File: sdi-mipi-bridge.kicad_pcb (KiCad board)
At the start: 6 copper layers, 70 x 42 mm, 204 parts, among them J1 112740-13, J2 112740-13, J3 WE_68715014522_ONE-SIDE, J4 GRPB052VWVN-RC, J5 GRPB041VWVN-RC, J6 GRPB052VWVN-RC, SW1 SW_DIP_x06, SW2 SW_DIP_x06, U1 MAX8902B, U2 GS2971A, U3 GS2988, U4 CrossLink_LIF-MD6000-6JMG80I, U5 SC18IS602BIPW, Y1 ABM7_27.000MH_D2Y_T

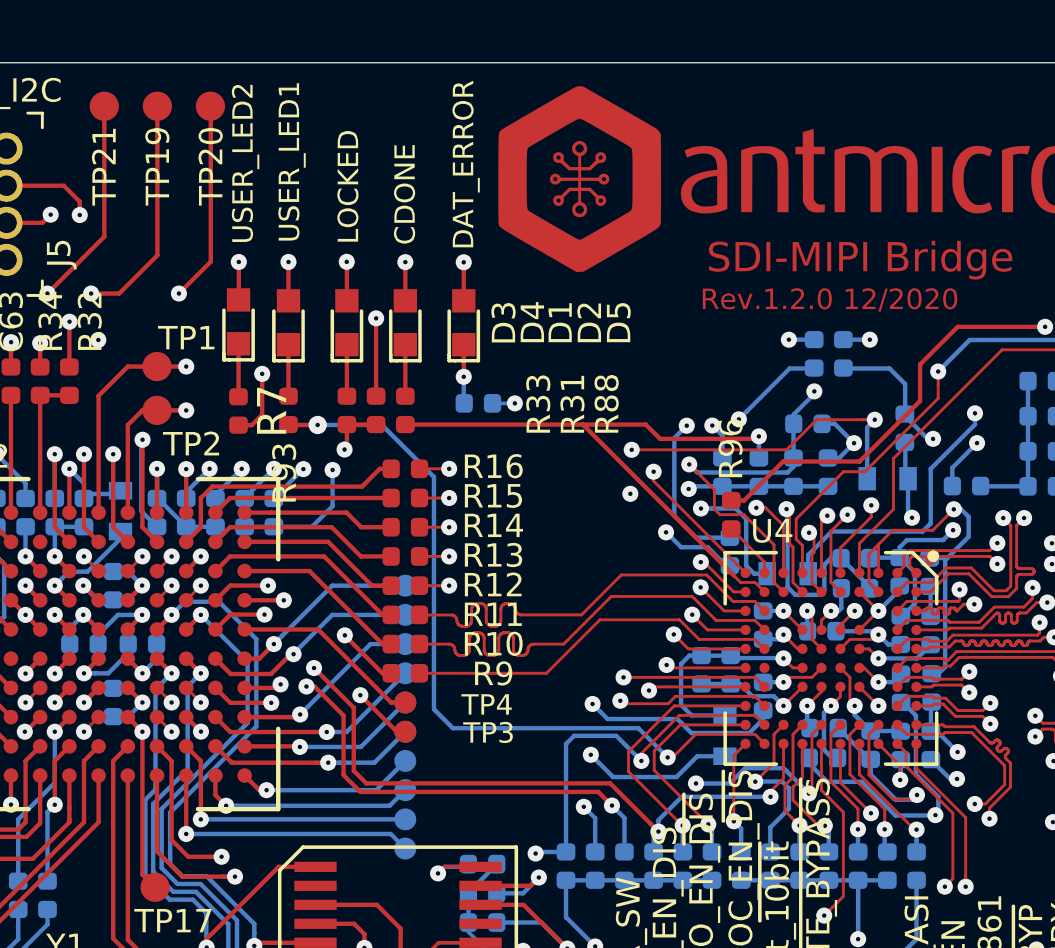
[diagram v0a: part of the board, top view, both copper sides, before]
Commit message: Change data pins routing
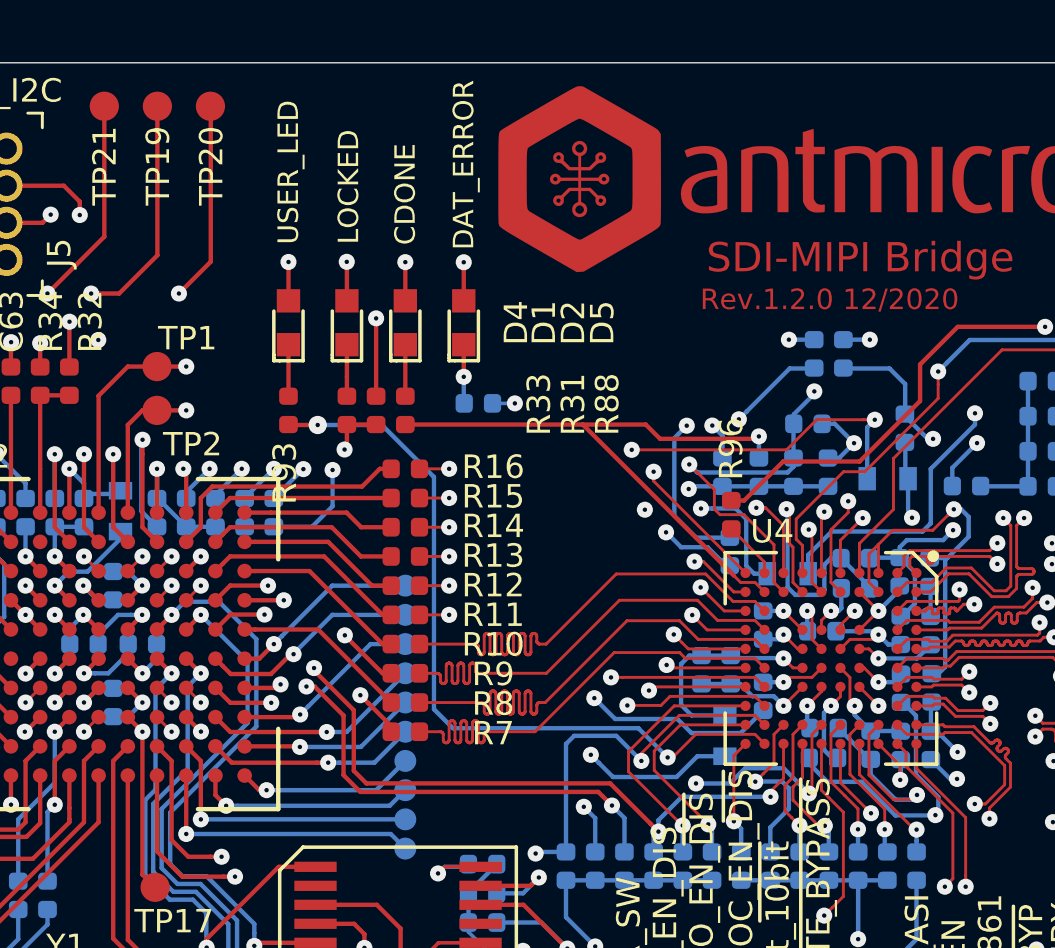
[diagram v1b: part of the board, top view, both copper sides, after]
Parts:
- removed D3: LG_L29K-G2J1-24-Z, sdi-mipi-bridge-footprints:LED_0603
- removed TP3, TP4: TP_SMD_0_75MM, sdi-mipi-bridge-footprints:Testpoint_smd_0_75mm
- added R8: R_0R_0402, sdi-mipi-bridge-footprints:0402-res, F.Cu at (131.0, 117.4)
- R7: value R_100R_0402 -> R_0R_0402
- moved R7 12.4 mm to (131.0, 118.4), turned to 180 degrees
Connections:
- net /USER_LED1 renamed /USER_LED
- R10 pad 1: /DOUT13 -> /DOUT14
- R10 pad 2: /D13 -> /D14
- R11 pad 1: /DOUT14 -> /DOUT10
- R11 pad 2: /D14 -> /D10
- R7 pad 1: Net-(D3-Pad1) -> /DOUT11
- R7 pad 2: /USER_LED2 -> /D11
- R9 pad 1: /DOUT12 -> /DOUT13
- R9 pad 2: /D12 -> /D13
- U2 pad C10: /D13 -> /D14
- U2 pad C8: /D12 -> /D13
- U2 pad C9: /D14 -> /D10
- U2 pad E10: Net-(TP4-Pad1) -> /D12
- U2 pad E9: Net-(TP3-Pad1) -> /D11
- U4 pad E1: /USER_LED2 -> /DOUT10
- U4 pad J6: Net-(U4-PadJ6) -> /DOUT11
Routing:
- net /USER_LED2: track 31.3 -> 0.00 mm, vias 2 -> 0
- net /DOUT10: track 0.00 -> 18.7 mm, vias 0 -> 2
- net /DOUT11: track 0.00 -> 17.8 mm
- net Net-(TP3-Pad1): track 8.37 -> 0.00 mm, vias 2 -> 0
- net /D11: track 0.00 -> 8.00 mm, vias 0 -> 2
- net /D10: track 0.00 -> 7.05 mm
- net /DOUT12: track 13.0 -> 19.7 mm
- net Net-(TP4-Pad1): track 6.53 -> 0.00 mm
- net /DOUT14: track 15.2 -> 19.7 mm
- net /DOUT19: track 13.2 -> 17.2 mm
- net /DOUT15: track 16.3 -> 20.2 mm
- net /DOUT16: track 15.3 -> 19.2 mm
- net /DOUT17: track 16.8 -> 20.6 mm
- net /DOUT18: track 15.8 -> 19.6 mm
- net /D13: track 6.05 -> 8.88 mm, vias 0 -> 2
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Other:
- board text added: "USER_LED"
- board text removed: "USER_LED1"
- board text removed: "USER_LED2"

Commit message: Update PCB, DRC clean
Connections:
- R10 pad 1: /DOUT14 -> /DOUT13
- R10 pad 2: /D14 -> /D13
- R11 pad 1: /DOUT10 -> /DOUT14
- R11 pad 2: /D10 -> /D14
- R7 pad 1: /DOUT11 -> /DOUT10
- R7 pad 2: /D11 -> /D10
- R8 pad 1: /DOUT12 -> /DOUT11
- R8 pad 2: /D12 -> /D11
- R9 pad 1: /DOUT13 -> /DOUT12
- R9 pad 2: /D13 -> /D12
- U2 pad C10: /D14 -> /D13
- U2 pad C8: /D13 -> /D12
- U2 pad C9: /D10 -> /D14
- U2 pad E10: /D12 -> /D11
- U2 pad E9: /D11 -> /D10
- U4 pad E1: /DOUT10 -> /DOUT14
- U4 pad J3: /DOUT14 -> /DOUT13
- U4 pad J4: /DOUT13 -> /DOUT12
- U4 pad J5: /DOUT12 -> /DOUT11
- U4 pad J6: /DOUT11 -> /DOUT10
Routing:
- net /D13: track 8.88 -> 6.05 mm, vias 2 -> 0
- net /D12: track 6.05 -> 8.88 mm, vias 0 -> 2
- net /DOUT13: track 16.9 -> 19.7 mm
- net /DOUT12: track 19.7 -> 16.9 mm
- net /D11: track 8.00 -> 6.05 mm, vias 2 -> 0
- net /DOUT11: track 17.8 -> 19.7 mm
- net /D14: track 6.05 -> 7.05 mm
- net /DOUT14: track 19.7 -> 18.7 mm, vias 0 -> 2
- net /DOUT10: track 18.7 -> 17.8 mm, vias 2 -> 0
- net /D10: track 7.05 -> 8.00 mm, vias 0 -> 2

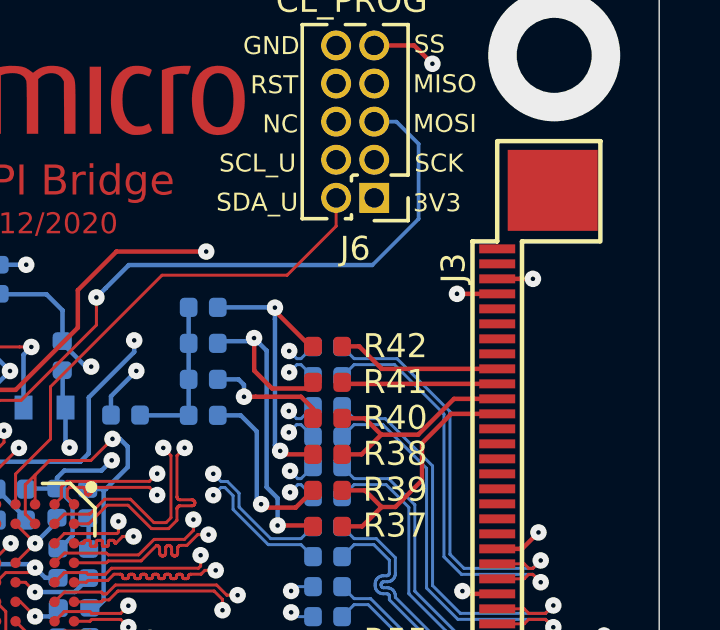
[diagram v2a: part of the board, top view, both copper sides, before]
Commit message: Add 0R resistor on 3.3v input to allow FFC to be disconnected from net
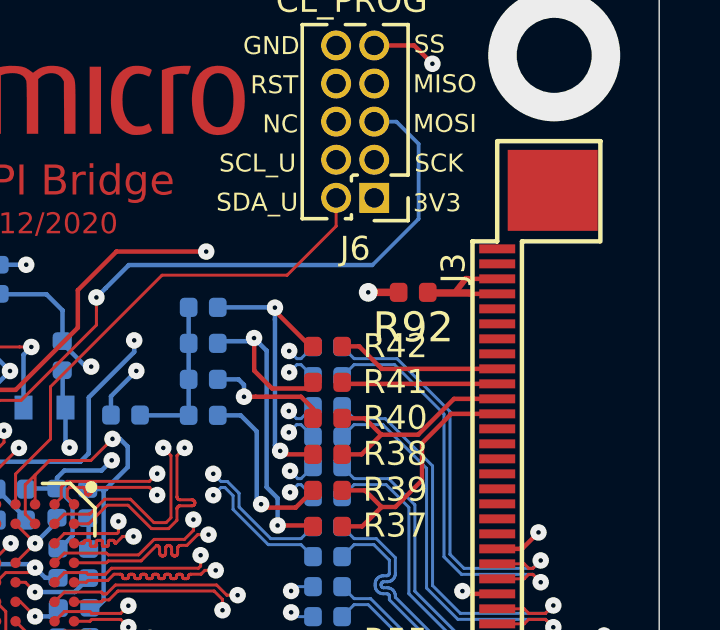
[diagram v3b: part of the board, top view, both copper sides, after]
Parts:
- added R92: R_0R_0402, sdi-mipi-bridge-footprints:0402-res, F.Cu at (159.8, 105.9)
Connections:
- J3 pad 47: +3V3 -> Net-(J3-Pad47)
- J3 pad 48: +3V3 -> Net-(J3-Pad47)
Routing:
- net Net-(J3-Pad47): track 0.00 -> 4.06 mm
- net +3V3: track 46.5 -> 45.0 mm, vias 16 -> 15

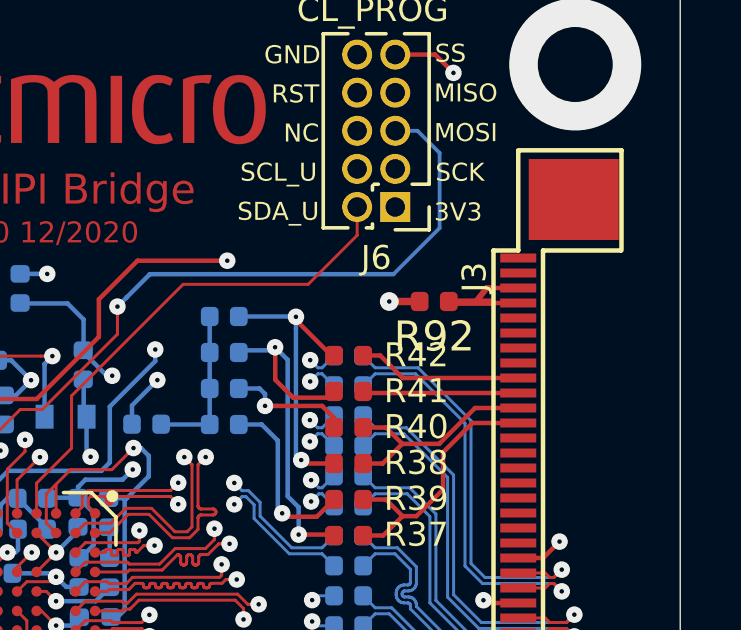
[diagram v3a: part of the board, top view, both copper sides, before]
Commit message: Increase 3.3v trace width, added 2nd via, increased via diameter
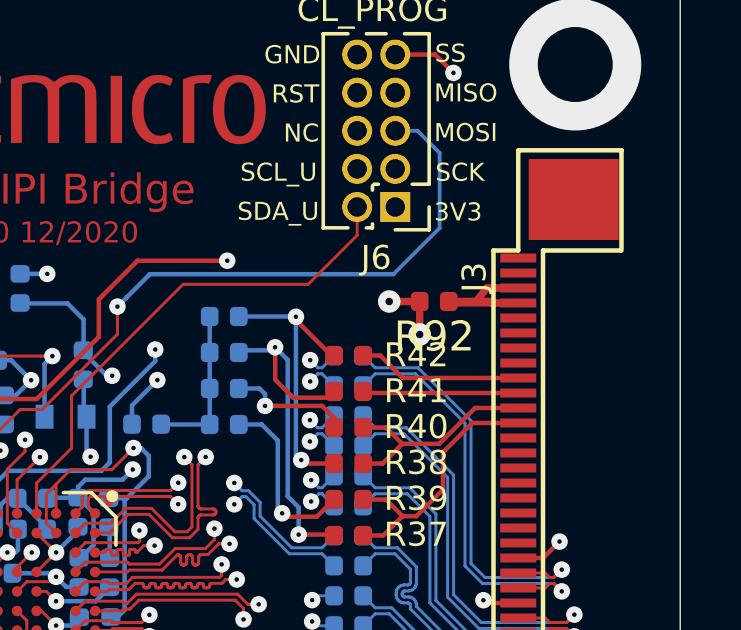
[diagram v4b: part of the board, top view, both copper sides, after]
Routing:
- net +3V3: track 45.0 -> 46.1 mm, vias 15 -> 16
